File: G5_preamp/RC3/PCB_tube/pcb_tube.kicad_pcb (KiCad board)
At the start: 2 copper layers, 100 x 47 mm, 31 parts, among them J1 PSU_TUBE, J2 PCB_TUBE, J3 OT

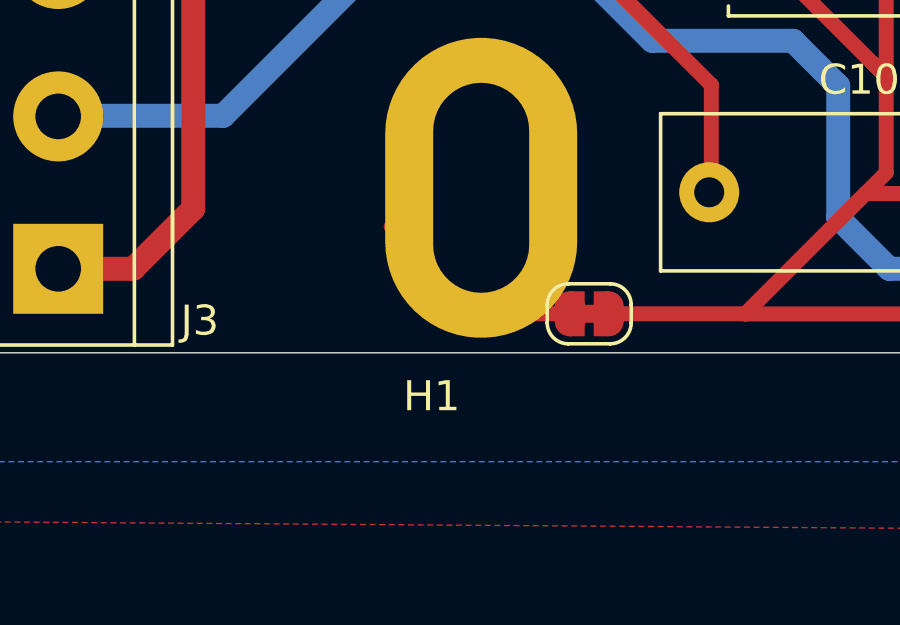
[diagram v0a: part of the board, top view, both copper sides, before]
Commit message: Pad fixation pcb_tube
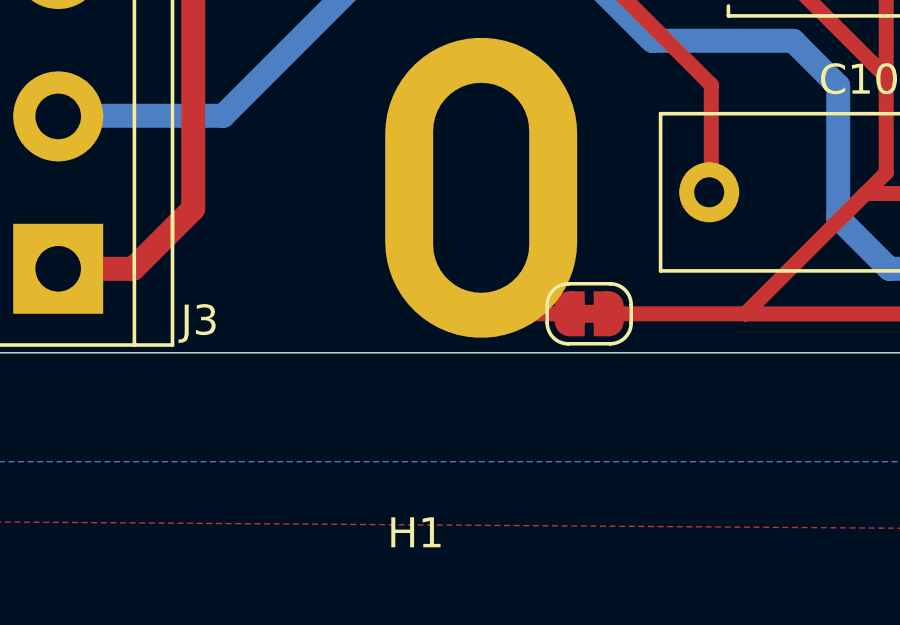
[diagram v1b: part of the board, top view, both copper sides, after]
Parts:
- moved H1 0.23 mm to (46.8, 105.8)
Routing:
- net GNDREF: track 7.10 -> 6.46 mm
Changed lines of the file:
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@@
   )
   (module MountingHole:MountingHole_3.2mm_M3 (layer F.Cu)
-    (at 46.95 105.65)
+    (at 46.75 105.76)
     (descr "Mounting Hole 3.2mm, no annular, M3")
     (tags "mounting hole 3.2mm no annular m3")
     (attr virtual)
-    (fp_text reference H1 (at 0 -4.2) (layer F.SilkS)
+    (fp_text reference H1 (at -0.33 0.26) (layer F.SilkS)
       (effects (font (size 1 1) (thickness 0.15)))
     )
@@
       (effects (font (size 1 1) (thickness 0.15)))
     )
-    (pad 1 thru_hole oval (at 1.65 -11.15) (size 6.4 10) (drill oval 3.2 7) (layers *.Cu *.Mask)
+    (pad 1 thru_hole oval (at 1.85 -11.26) (size 6.4 10) (drill oval 3.2 7) (layers *.Cu *.Mask)
       (net 13 GNDREF) (zone_connect 2))
   )
@@
   (segment (start 90.58 84) (end 90.58 82.18) (width 0.5) (layer F.Cu) (net 12))
   (segment (start 90.58 82.18) (end 89.7 81.3) (width 0.5) (layer F.Cu) (net 12))
-  (segment (start 46.8 95.8) (end 45.6 95.8) (width 0.5) (layer F.Cu) (net 13))
+  (segment (start 48.62 97.62) (end 48.62 94.49) (width 0.5) (layer F.Cu) (net 13))
   (segment (start 51.5 98.7) (end 49.7 98.7) (width 0.5) (layer F.Cu) (net 13))
-  (segment (start 49.7 98.7) (end 46.8 95.8) (width 0.5) (layer F.Cu) (net 13))
+  (segment (start 49.7 98.7) (end 48.62 97.62) (width 0.5) (layer F.Cu) (net 13))
   (segment (start 80.1 81.3) (end 82.1 83.3) (width 0.5) (layer B.Cu) (net 14))
   (segment (start 88.1 86.1) (end 88.1 84) (width 0.5) (layer B.Cu) (net 14))

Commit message: mod pcb_tube
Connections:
- C10 pad 3: (no net) -> GNDS
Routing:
- net GNDS: track 182.5 -> 181.6 mm
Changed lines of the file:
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@@
   (title_block
     (title "Preamp G5 with Pistortion System")
-    (date 2019-04-25)
-    (rev RC2)
+    (date 2019-05-07)
+    (rev RC3)
     (company http://www.projetg5.com)
     (comment 2 "Licence under Creative Commons BY-NC-SA 4.0")
@@
     (39 F.Mask user)
     (40 Dwgs.User user)
-    (41 Cmts.User user)
+    (41 Cmts.User user hide)
     (42 Eco1.User user)
     (43 Eco2.User user)
@@
     (mod_text_size 1 1)
     (mod_text_width 0.15)
-    (pad_size 6.4 10)
-    (pad_drill 3.2)
+    (pad_size 2 2)
+    (pad_drill 1)
     (pad_to_mask_clearance 0.051)
     (solder_mask_min_width 0.25)
     (aux_axis_origin 30 100)
     (grid_origin 30 100)
-    (visible_elements 7FFFFFFF)
+    (visible_elements 7FFFFF7F)
     (pcbplotparams
       (layerselection 0x010f0_ffffffff)
@@
     (pad 1 thru_hole circle (at 0 0) (size 2 2) (drill 1) (layers *.Cu *.Mask)
       (net 21 "Net-(C10-Pad1)"))
-    (pad 3 thru_hole circle (at 7.5 0) (size 2 2) (drill 1) (layers *.Cu *.Mask))
+    (pad 3 thru_hole circle (at 7.5 0) (size 2 2) (drill 1) (layers *.Cu *.Mask)
+      (net 2 GNDS))
     (model ${KISYS3DMOD}/Capacitor_THT.3dshapes/C_Rect_L13.0mm_W5.0mm_P10.00mm_FKS3_FKP3_MKS4.wrl
       (at (xyz 0 0 0))
@@
     (tags "mounting hole 3.2mm no annular m3")
     (attr virtual)
-    (fp_text reference H1 (at -0.33 0.26) (layer F.SilkS)
+    (fp_text reference H1 (at -0.33 0.26) (layer F.SilkS) hide
       (effects (font (size 1 1) (thickness 0.15)))
     )
@@
   (segment (start 57.4 98.7) (end 57.405457 98.705457) (width 0.5) (layer F.Cu) (net 2))
   (segment (start 57.405457 98.705457) (end 67.594543 98.705457) (width 0.5) (layer F.Cu) (net 2))
-  (segment (start 60.45 95.65) (end 57.4 98.7) (width 0.5) (layer F.Cu) (net 2))
   (segment (start 74.894543 98.705457) (end 67.594543 98.705457) (width 0.5) (layer F.Cu) (net 2))
   (segment (start 119.194543 98.705457) (end 74.894543 98.705457) (width 0.5) (layer F.Cu) (net 2))
@@
   (segment (start 58.7 87.4) (end 56.3 87.4) (width 0.5) (layer F.Cu) (net 2))
   (segment (start 62.1 90.8) (end 58.7 87.4) (width 0.5) (layer F.Cu) (net 2))
-  (segment (start 62.1 94) (end 60.45 95.65) (width 0.5) (layer F.Cu) (net 2))
   (segment (start 61.641254 90.341254) (end 62.1 90.8) (width 0.5) (layer F.Cu) (net 2))
-  (segment (start 62.1 90.8) (end 62.1 94) (width 0.5) (layer F.Cu) (net 2))
   (segment (start 62.1 84.6) (end 62.1 90.8) (width 0.5) (layer F.Cu) (net 2))
   (segment (start 63.92 84) (end 62.7 84) (width 0.5) (layer F.Cu) (net 2))
   (segment (start 62.7 84) (end 62.1 84.6) (width 0.5) (layer F.Cu) (net 2))
-  (segment (start 61.41 94.69) (end 60.45 95.65) (width 0.5) (layer F.Cu) (net 2))
-  (segment (start 66.16 94.69) (end 61.41 94.69) (width 0.5) (layer F.Cu) (net 2))
   (segment (start 55.57 54.53) (end 55.57 56.36) (width 0.5) (layer F.Cu) (net 2))
   (segment (start 60.5 54.1) (end 56 54.1) (width 0.5) (layer F.Cu) (net 2))
@@
   (segment (start 78.5 84.4) (end 78.5 91.9) (width 0.5) (layer F.Cu) (net 2))
   (segment (start 78.5 91.9) (end 77.06 93.34) (width 0.5) (layer F.Cu) (net 2))
+  (segment (start 62.1 93.1) (end 63.7 94.7) (width 0.5) (layer F.Cu) (net 2))
+  (segment (start 62.1 90.8) (end 62.1 93.1) (width 0.5) (layer F.Cu) (net 2))
+  (segment (start 59.63 98.7) (end 57.4 98.7) (width 0.5) (layer F.Cu) (net 2))
+  (segment (start 66.16 94.69) (end 63.64 94.69) (width 0.5) (layer F.Cu) (net 2))
+  (segment (start 63.64 94.69) (end 59.63 98.7) (width 0.5) (layer F.Cu) (net 2))
   (segment (start 64.7 77.1) (end 67.4 79.8) (width 0.5) (layer B.Cu) (net 3))
   (segment (start 59.4 77.1) (end 64.7 77.1) (width 0.5) (layer B.Cu) (net 3))
